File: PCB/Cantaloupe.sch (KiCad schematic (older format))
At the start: 125 parts, among them J1 USB_In, J2 OLED, J3 Link, J4 Debug, J5 Trackball, Q1 2N7002, Q2 AO3401A, SW1 MX, SW10 MX, SW11 MX, SW12 MX, SW13 MX, SW14 MX, SW15 MX, SW16 MX, SW17 MX, SW18 MX, SW19 MX, SW2 MX, SW20 MX, SW21 MX, SW22 MX, SW23 MX, SW24 MX, SW25 MX, SW26 MX, SW27 MX, SW28 MX, SW29 MX, SW3 MX, SW30 MX, SW31 Encoder, SW32 MX, SW4 MX, SW5 MX, SW6 MX, SW7 MX, SW8 MX, SW9 MX, U1 STM32F303CCTx, U2 SRV05-4, U3 SRV05-4, U4 XC6206P332MR, U5 LMV321, Y1 8MHz

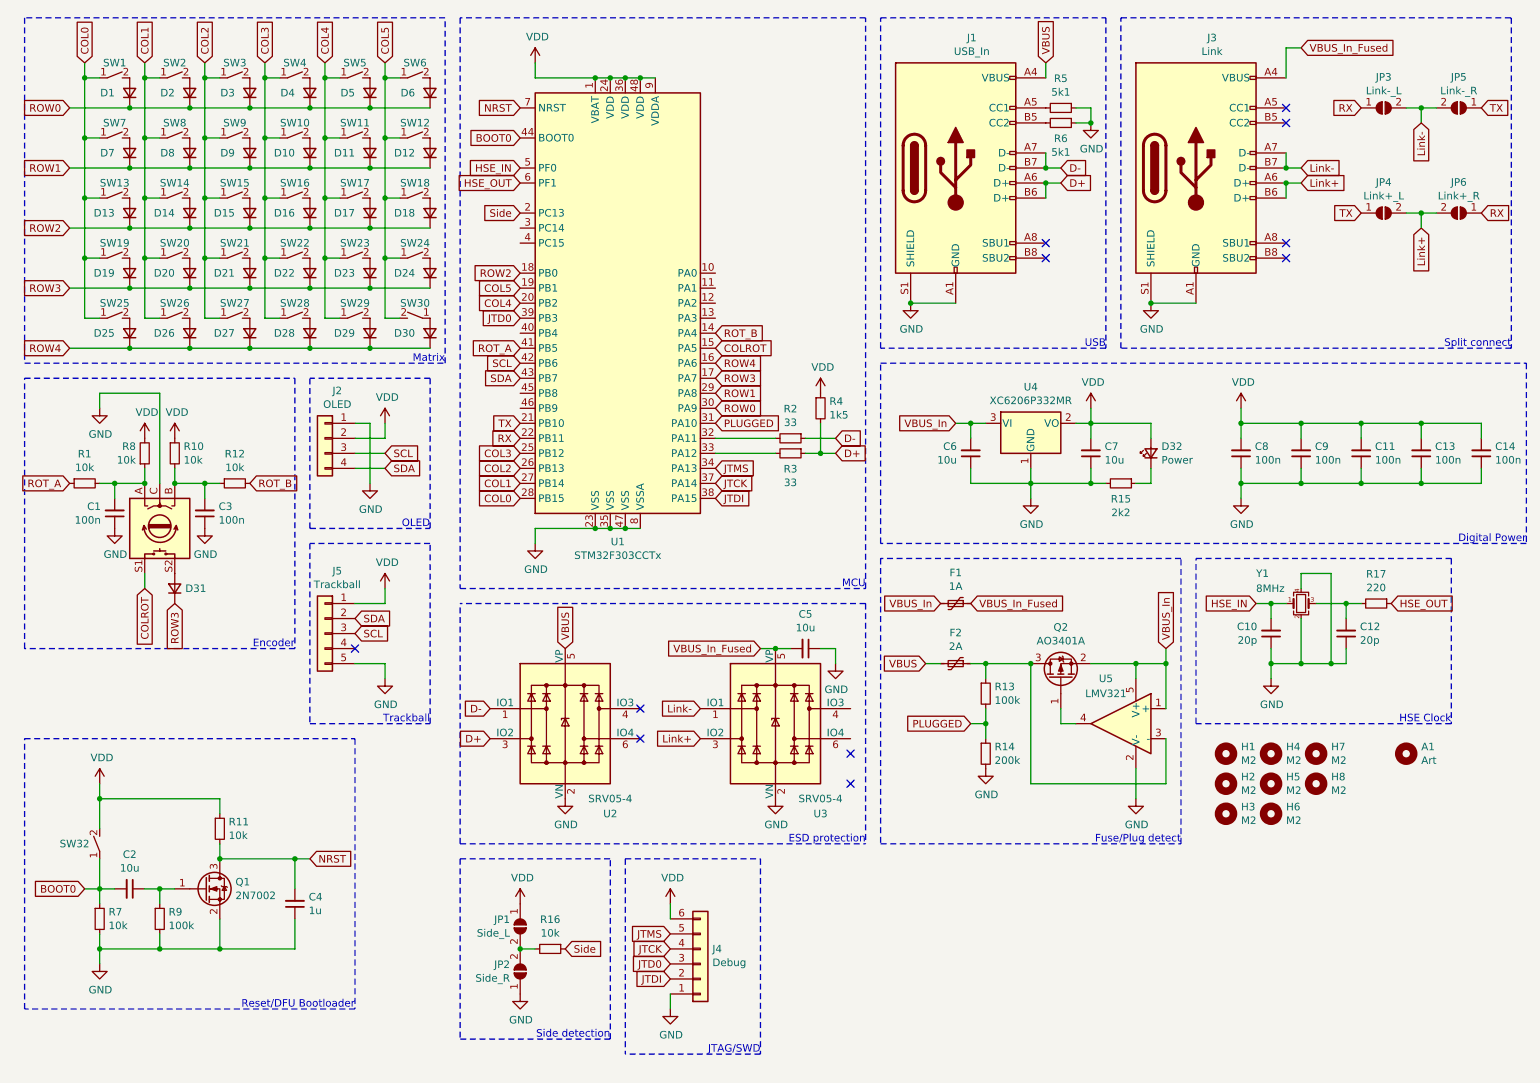
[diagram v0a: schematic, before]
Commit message: 20/1/2022 update
Cleaned up read-me. Rearranged location of mounting holes and changed size of holes. Rerouted some traces. Cleaned up silkscreen. Added DXF files for plate and base. Changed images. Added BOM.
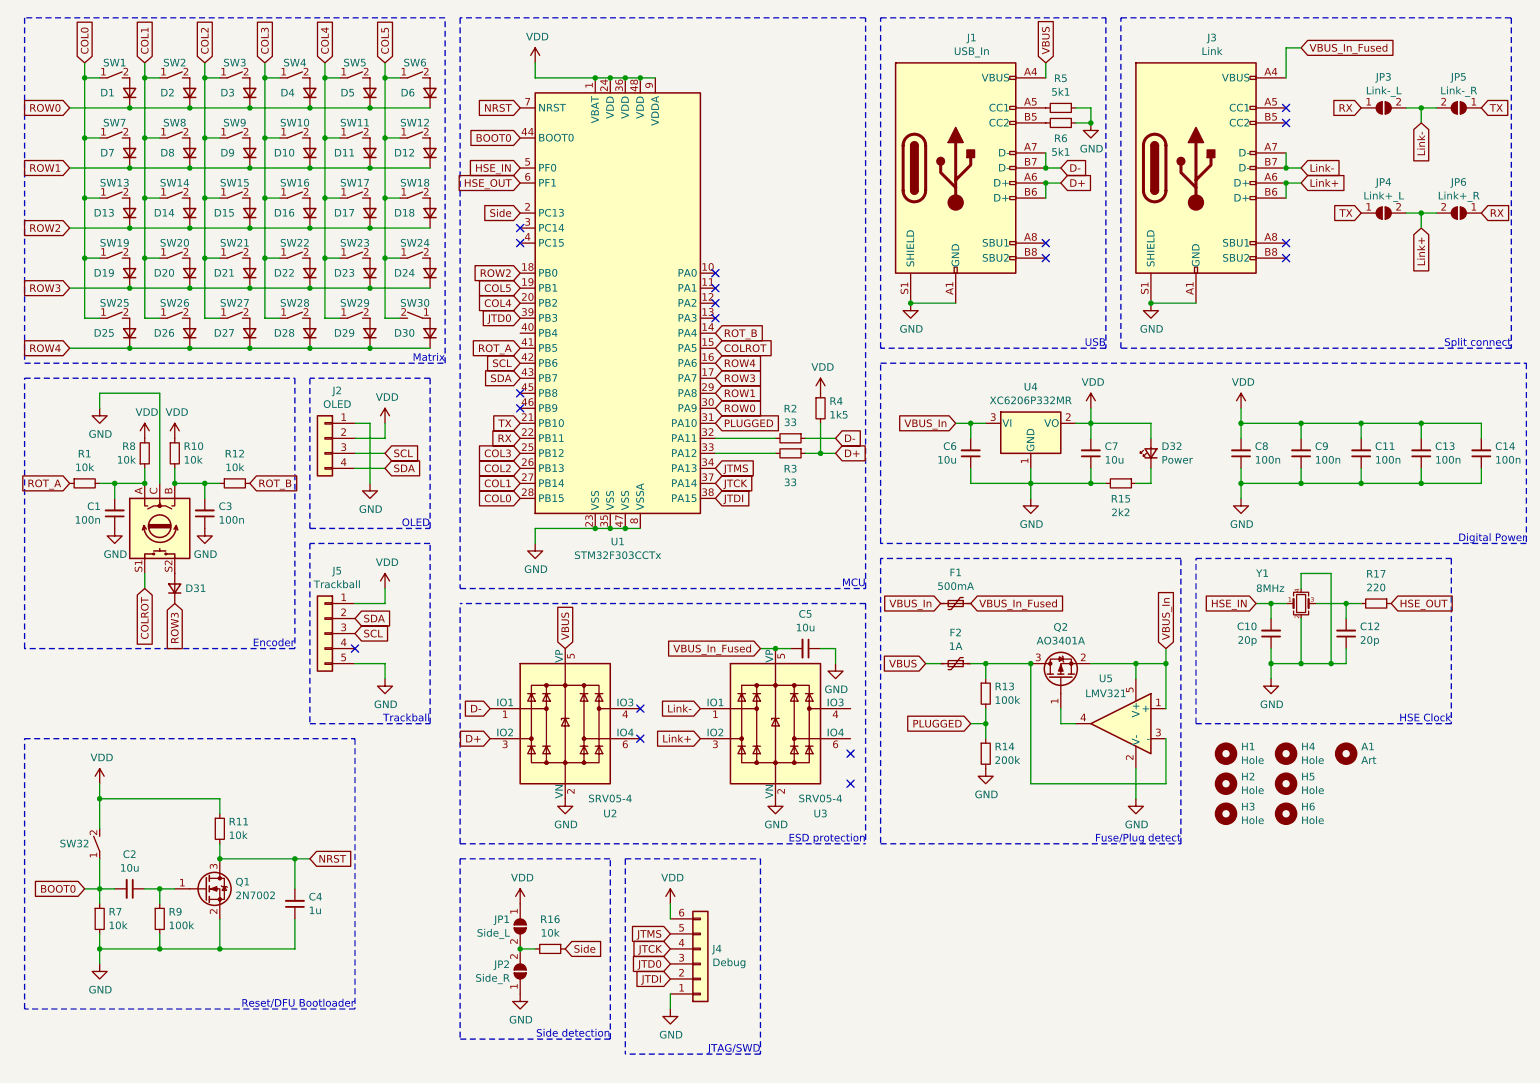
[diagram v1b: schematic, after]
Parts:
- removed H7, H8: M2, Ariamelon:MountingHole_2.2mm_M2_Pad, symbol Mechanical:MountingHole
- F1: value 1A -> 500mA
- F2: value 2A -> 1A
- H1, H2, H3, H4, H5, H6: value M2 -> Hole; footprint Ariamelon:MountingHole_2.2mm_M2_Pad -> Ariamelon:HOLE_M2_TH
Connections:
- no-connect marks 11 -> 19
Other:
- moved on the sheet: A1, H4, H5, H6
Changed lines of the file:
@@
 P 6900 4900
 F 0 "F2" V 6695 4900 50  0000 C CNN
-F 1 "2A" V 6786 4900 50  0000 C CNN
+F 1 "1A" V 6786 4900 50  0000 C CNN
 F 2 "Fuse:Fuse_1206_3216Metric" H 6950 4700 50  0001 L CNN
 F 3 "~" H 6900 4900 50  0001 C CNN
@@
 P 6900 4500
 F 0 "F1" V 6695 4500 50  0000 C CNN
-F 1 "1A" V 6786 4500 50  0000 C CNN
+F 1 "500mA" V 6786 4500 50  0000 C CNN
 F 2 "Fuse:Fuse_1206_3216Metric" H 6950 4300 50  0001 L CNN
 F 3 "~" H 6900 4500 50  0001 C CNN
@@
 P 8700 5500
 F 0 "H1" H 8800 5546 50  0000 L CNN
-F 1 "M2" H 8800 5455 50  0000 L CNN
-F 2 "Ariamelon:MountingHole_2.2mm_M2_Pad" H 8700 5500 50  0001 C CNN
+F 1 "Hole" H 8800 5455 50  0000 L CNN
+F 2 "Ariamelon:HOLE_M2_TH" H 8700 5500 50  0001 C CNN
 F 3 "~" H 8700 5500 50  0001 C CNN
 	1    8700 5500
@@
 P 8700 5700
 F 0 "H2" H 8800 5746 50  0000 L CNN
-F 1 "M2" H 8800 5655 50  0000 L CNN
-F 2 "Ariamelon:MountingHole_2.2mm_M2_Pad" H 8700 5700 50  0001 C CNN
+F 1 "Hole" H 8800 5655 50  0000 L CNN
+F 2 "Ariamelon:HOLE_M2_TH" H 8700 5700 50  0001 C CNN
 F 3 "~" H 8700 5700 50  0001 C CNN
 	1    8700 5700
@@
 P 8700 5900
 F 0 "H3" H 8800 5946 50  0000 L CNN
-F 1 "M2" H 8800 5855 50  0000 L CNN
-F 2 "Ariamelon:MountingHole_2.2mm_M2_Pad" H 8700 5900 50  0001 C CNN
+F 1 "Hole" H 8800 5855 50  0000 L CNN
+F 2 "Ariamelon:HOLE_M2_TH" H 8700 5900 50  0001 C CNN
 F 3 "~" H 8700 5900 50  0001 C CNN
 	1    8700 5900
@@
 L Mechanical:MountingHole H4
 U 1 1 62097F05
-P 9000 5500
-F 0 "H4" H 9100 5546 50  0000 L CNN
-F 1 "M2" H 9100 5455 50  0000 L CNN
-F 2 "Ariamelon:MountingHole_2.2mm_M2_Pad" H 9000 5500 50  0001 C CNN
-F 3 "~" H 9000 5500 50  0001 C CNN
-	1    9000 5500
+P 9100 5500
+F 0 "H4" H 9200 5546 50  0000 L CNN
+F 1 "Hole" H 9200 5455 50  0000 L CNN
+F 2 "Ariamelon:HOLE_M2_TH" H 9100 5500 50  0001 C CNN
+F 3 "~" H 9100 5500 50  0001 C CNN
+	1    9100 5500
 	1    0    0    -1
 $EndComp
@@
 L Mechanical:MountingHole H5
 U 1 1 62097F0B
-P 9000 5700
-F 0 "H5" H 9100 5746 50  0000 L CNN
-F 1 "M2" H 9100 5655 50  0000 L CNN
-F 2 "Ariamelon:MountingHole_2.2mm_M2_Pad" H 9000 5700 50  0001 C CNN
-F 3 "~" H 9000 5700 50  0001 C CNN
-	1    9000 5700
+P 9100 5700
+F 0 "H5" H 9200 5746 50  0000 L CNN
+F 1 "Hole" H 9200 5655 50  0000 L CNN
+F 2 "Ariamelon:HOLE_M2_TH" H 9100 5700 50  0001 C CNN
+F 3 "~" H 9100 5700 50  0001 C CNN
+	1    9100 5700
 	1    0    0    -1
 $EndComp
@@
 L Mechanical:MountingHole H6
 U 1 1 62097F11
-P 9000 5900
-F 0 "H6" H 9100 5946 50  0000 L CNN
-F 1 "M2" H 9100 5855 50  0000 L CNN
-F 2 "Ariamelon:MountingHole_2.2mm_M2_Pad" H 9000 5900 50  0001 C CNN
-F 3 "~" H 9000 5900 50  0001 C CNN
-	1    9000 5900
+P 9100 5900
+F 0 "H6" H 9200 5946 50  0000 L CNN
+F 1 "Hole" H 9200 5855 50  0000 L CNN
+F 2 "Ariamelon:HOLE_M2_TH" H 9100 5900 50  0001 C CNN
+F 3 "~" H 9100 5900 50  0001 C CNN
+	1    9100 5900
 	1    0    0    -1
 $EndComp
@@
 L Mechanical:MountingHole A1
 U 1 1 620A77CC
-P 9900 5500
-F 0 "A1" H 10000 5546 50  0000 L CNN
-F 1 "Art" H 10000 5455 50  0000 L CNN
-F 2 "Ariamelon:Catmelon" H 9900 5500 50  0001 C CNN
-F 3 "~" H 9900 5500 50  0001 C CNN
-	1    9900 5500
+P 9500 5500
+F 0 "A1" H 9600 5546 50  0000 L CNN
+F 1 "Art" H 9600 5455 50  0000 L CNN
+F 2 "Ariamelon:Catmelon" H 9500 5500 50  0001 C CNN
+F 3 "~" H 9500 5500 50  0001 C CNN
+	1    9500 5500
 	1    0    0    -1
 $EndComp
@@
 Text GLabel 5300 2800 2    50   Input ~ 0
 COLROT
-$Comp
-L Mechanical:MountingHole H7
-U 1 1 62449F60
-P 9300 5500
-F 0 "H7" H 9400 5546 50  0000 L CNN
-F 1 "M2" H 9400 5455 50  0000 L CNN
-F 2 "Ariamelon:MountingHole_2.2mm_M2_Pad" H 9300 5500 50  0001 C CNN
-F 3 "~" H 9300 5500 50  0001 C CNN
-	1    9300 5500
-	1    0    0    -1
-$EndComp
 Text GLabel 5300 2700 2    50   Input ~ 0
 ROT_B
-$Comp
-L Mechanical:MountingHole H8
-U 1 1 62450530
-P 9300 5700
-F 0 "H8" H 9400 5746 50  0000 L CNN
-F 1 "M2" H 9400 5655 50  0000 L CNN
-F 2 "Ariamelon:MountingHole_2.2mm_M2_Pad" H 9300 5700 50  0001 C CNN
-F 3 "~" H 9300 5700 50  0001 C CNN
-	1    9300 5700
-	1    0    0    -1
-$EndComp
+NoConn ~ 4000 2000
+NoConn ~ 4000 2100
+NoConn ~ 5300 2300
+NoConn ~ 5300 2400
+NoConn ~ 5300 2500
+NoConn ~ 5300 2600
+NoConn ~ 4000 3100
+NoConn ~ 4000 3200
 $EndSCHEMATC

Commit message: STM32F4x0 version
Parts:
- removed R4: 1k5, Resistor_SMD:R_0603_1608Metric, symbol Device:R_Small
- removed U1: STM32F303CCTx, Package_QFP:LQFP-48_7x7mm_P0.5mm, symbol MCU_ST_STM32F3:STM32F303CCTx
- added C15: 4.7u, Capacitor_SMD:C_0603_1608Metric, symbol Device:C_Small
- added L1: 10u, Inductor_SMD:L_0603_1608Metric, symbol Device:L_Small
- added U1: STM32F4x1CxUx, Package_DFN_QFN:QFN-48-1EP_7x7mm_P0.5mm_EP5.6x5.6mm, symbol MCU_ST_STM32F4:STM32F411CCUx
- R2, R3: value 33 -> 10
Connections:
- net BOOT0: now also R7.2, U1.44 (BOOT0); no longer R7.1
- net COL0: now also U1.26 (PB13)
- net COL1: now also U1.25 (PB12)
- net COL2: now also U1.21 (PB10)
- net COL3: now also U1.20 (PB2)
- net COL4: now also U1.19 (PB1)
- net COL5: now also U1.18 (PB0)
- net COLROT: now also U1.13 (PA3)
- net GND: now also J4.6 (Pin_6), R7.1, C15.1, U1.23 (VSS), U1.35 (VSS), U1.47 (VSS), U1.49 (VSS), U1.8 (VSSA); no longer J4.1 (Pin_1), R7.2
- net HSE_IN: now also U1.5 (PH0)
- net HSE_OUT: now also U1.6 (PH1)
- net JTCK: now also J4.3 (Pin_3), U1.37 (PA14); no longer J4.4 (Pin_4)
- net JTD0: now also J4.4 (Pin_4), U1.39 (PB3); no longer J4.3 (Pin_3)
- net JTDI: now also J4.5 (Pin_5), U1.38 (PA15); no longer J4.2 (Pin_2)
- net JTMS: now also J4.2 (Pin_2), U1.34 (PA13); no longer J4.5 (Pin_5)
- net NRST: now also U1.7 (NRST)
- net PLUGGED: now also U1.29 (PA8)
- net ROT_A: now also U1.41 (PB5)
- net ROT_B: now also U1.14 (PA4)
- net ROW0: now also U1.28 (PB15)
- net ROW1: now also U1.27 (PB14)
- net ROW2: now also U1.17 (PA7)
- net ROW3: now also U1.16 (PA6)
- net ROW4: now also U1.15 (PA5)
- net RX: now also U1.31 (PA10)
- net SCL: now also U1.42 (PB6)
- net SDA: now also U1.43 (PB7)
- net Side: now also U1.2 (PC13)
- net TX: now also U1.30 (PA9)
- net VDD: now also J4.1 (Pin_1), L1.2, U1.1 (VBAT), U1.24 (VDD), U1.36 (VDD), U1.48 (VDD); no longer J4.6 (Pin_6)
- net at R2.2: now also U1.32 (PA11)
- net at R3.2: now also U1.33 (PA12)
- new net: C15.2, U1.22 (VCAP1)
- new net: L1.1, U1.9 (VDDA)
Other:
- moved on the sheet: C2, C4, C5, J4, J5, JP1, JP2, Q1, R11, R16, R2, R3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

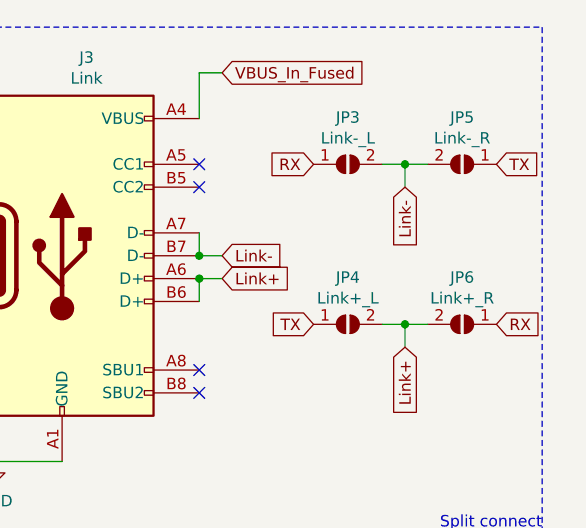
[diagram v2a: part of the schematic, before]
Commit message: Did some rerouting, increased clearances and via size, updated footprint master
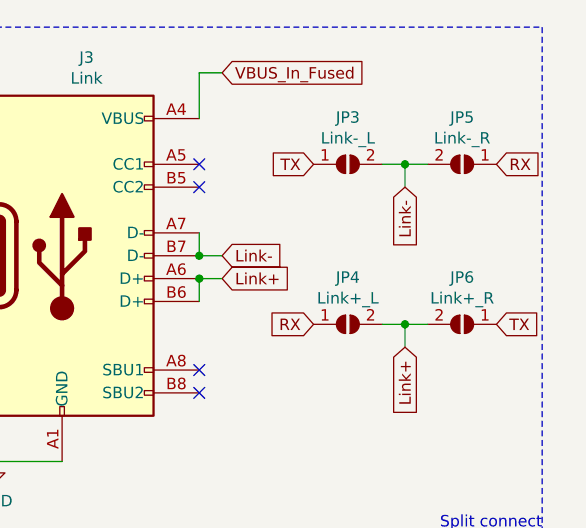
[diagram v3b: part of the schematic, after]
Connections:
- net RX: now also JP4.1 (A), JP5.1 (A); no longer JP3.1 (A), JP6.1 (A)
- net TX: now also JP3.1 (A), JP6.1 (A); no longer JP4.1 (A), JP5.1 (A)
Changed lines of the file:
@@
 Wire Notes Line
 	8000 600  10600 600
-Wire Notes Line
-	10600 600  10600 2800
 Wire Wire Line
 	10000 1200 10100 1200
@@
 	-1   0    0    -1
 $EndComp
-Text GLabel 10400 1900 2    50   Input ~ 0
-RX
-Text GLabel 9600 1200 0    50   Input ~ 0
+Text GLabel 10400 1200 2    50   Input ~ 0
 RX
 $Comp
@@
 	1    0    0    -1
 $EndComp
-Text GLabel 9600 1900 0    50   Input ~ 0
-TX
-Text GLabel 10400 1200 2    50   Input ~ 0
+Text GLabel 10400 1900 2    50   Input ~ 0
 TX
 Text GLabel 10000 2000 3    50   Input ~ 0
@@
 NoConn ~ 5600 2500
 NoConn ~ 5600 2600
+Text GLabel 9600 1200 0    50   Input ~ 0
+TX
+Text GLabel 9600 1900 0    50   Input ~ 0
+RX
+Wire Notes Line
+	10600 600  10600 2800
 $EndSCHEMATC
